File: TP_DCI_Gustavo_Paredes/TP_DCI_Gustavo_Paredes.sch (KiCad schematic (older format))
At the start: 32 parts, among them J101 Conector, J102 DB9 Hembra, J103 DB9 Macho, J104 Conector +5V, U101 LTC1485, U102 LTC1485

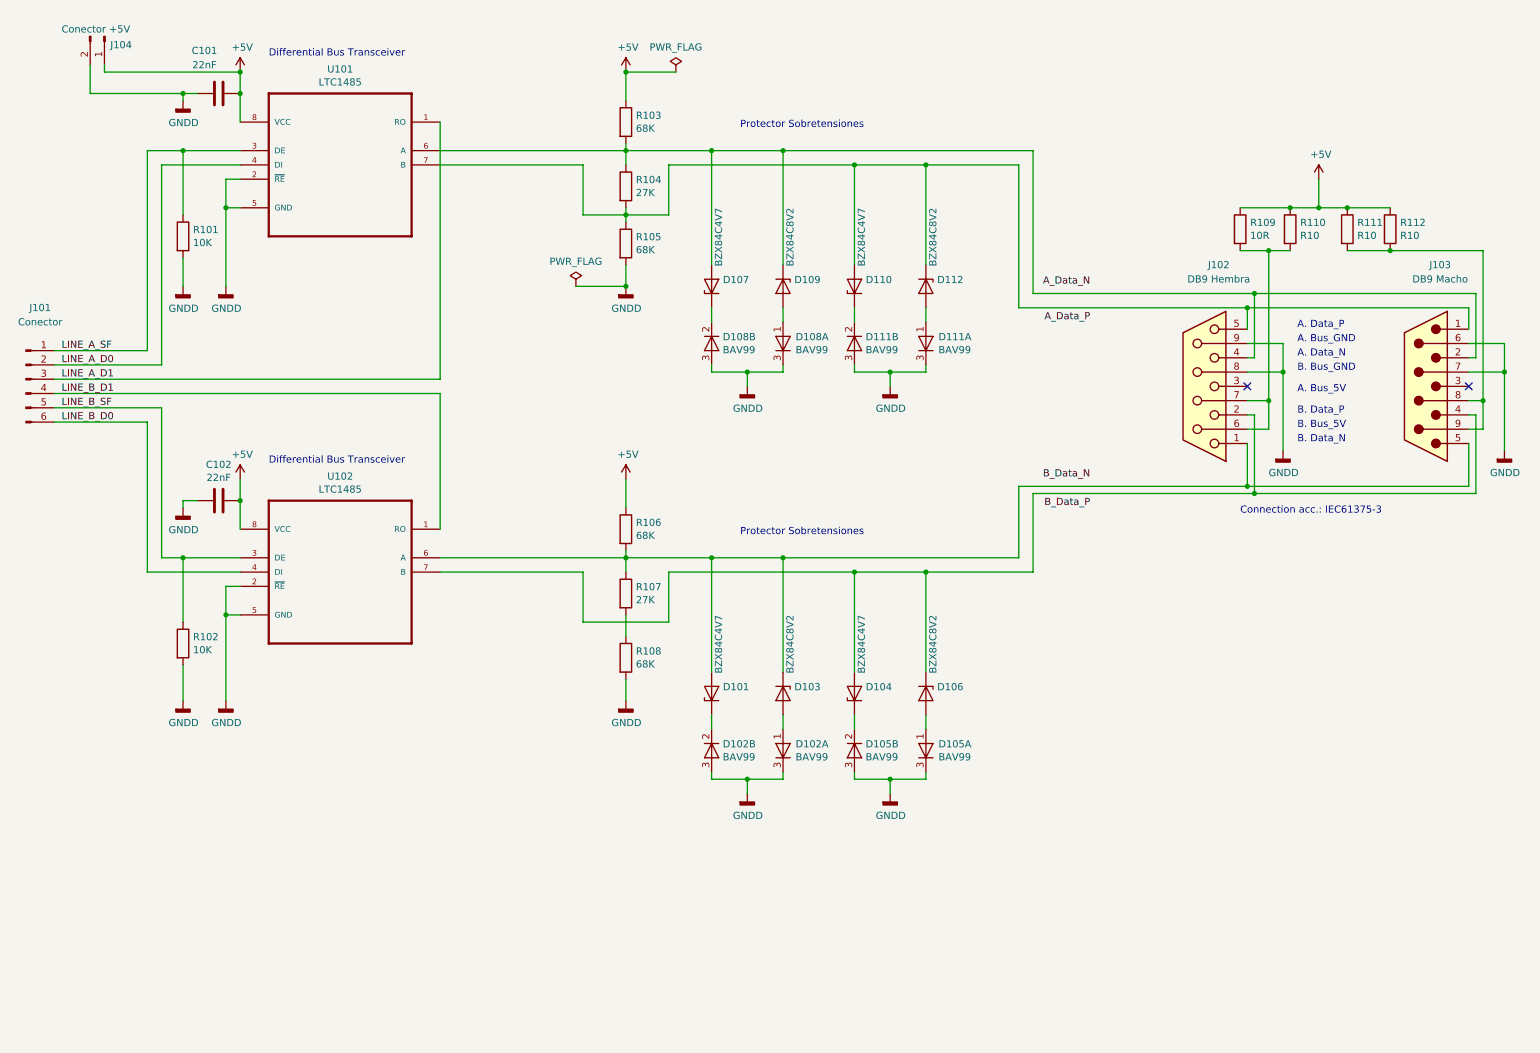
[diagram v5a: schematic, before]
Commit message: Correcciones Esquematico V3
Se realizaron las correcciones menores que el Docente indico. Se actualizo huella y 3D del LTC1485 y los dos DB9.
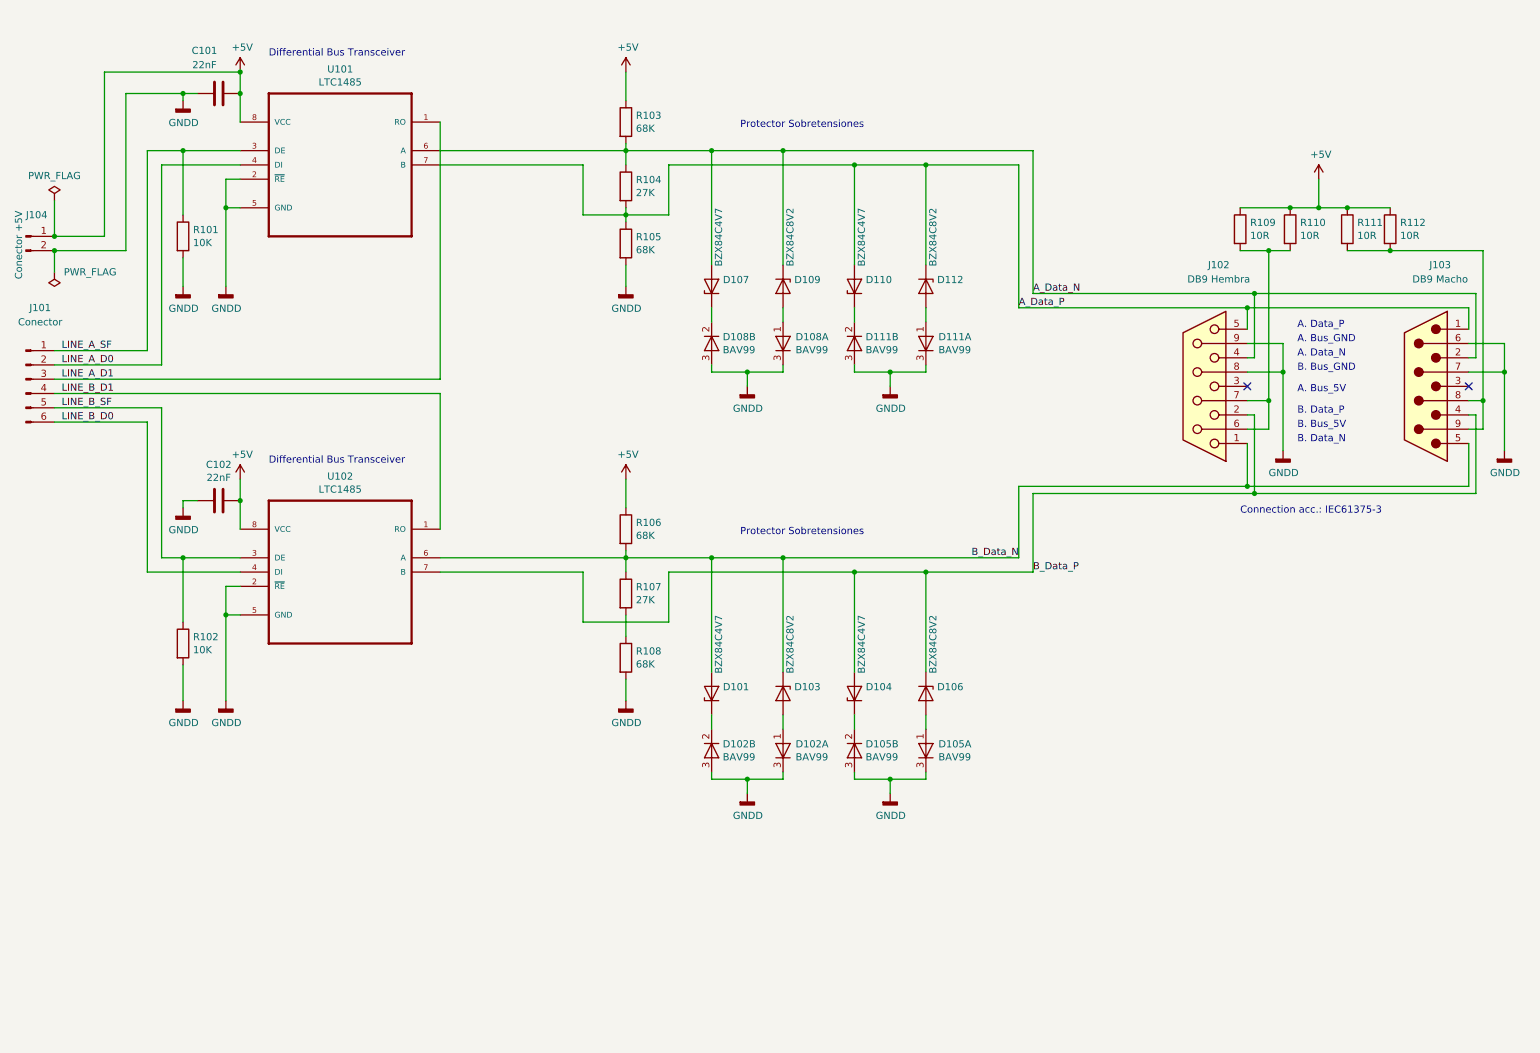
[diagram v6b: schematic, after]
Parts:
- J101: footprint Connector_PinHeader_1.00mm:PinHeader_1x06_P1.00mm_Vertical -> Connector_PinHeader_2.54mm:PinHeader_1x06_P2.54mm_Vertical
- J104: footprint Connector_PinHeader_1.00mm:PinHeader_1x02_P1.00mm_Vertical -> Connector_PinHeader_2.54mm:PinHeader_1x02_P2.54mm_Vertical
- R110, R111, R112: value R10 -> 10R
- U101, U102: footprint LTC1485IS8PBF:SOIC127P600X175-8N -> Package_DIP:DIP-8_W7.62mm_LongPads
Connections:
- net A_Data_N: now also D107.2 (A), D109.1 (K), J102.4, J103.2, R103.2, R104.1, U101.6 (A)
- net A_Data_P: now also D110.2 (A), D112.1 (K), J102.5, J103.1, R104.2, R105.1, U101.7 (B)
- net B_Data_N: now also D101.2 (A), D103.1 (K), J102.1, J103.5, R106.2, R107.1, U102.6 (A)
- net B_Data_P: now also D104.2 (A), D106.1 (K), J102.2, J103.4, U102.7 (B)
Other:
- moved on the sheet: J104
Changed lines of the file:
@@
 Sheet 1 1
 Title "KP99S RS485 PORT - Pagina 7/7"
-Date "2019-06-17"
-Rev "V2"
-Comp "CESE UBA - 7ma Cohorte"
+Date "2019-07-02"
+Rev "V3"
+Comp "DCI - CESE UBA - 7ma Cohorte"
 Comment1 "Autor: Gustavo Fabian Paredes Delaloye"
 Comment2 "Revisor: Julian Bustamante"
-Comment3 ""
+Comment3 "Licencia: GPL"
 Comment4 ""
 $EndDescr
@@
 F 0 "U101" H 2850 2170 50  0000 C CNN
 F 1 "LTC1485" H 2850 2079 50  0000 C CNN
-F 2 "LTC1485IS8PBF:SOIC127P600X175-8N" H 2850 1600 50  0001 L BNN
+F 2 "Package_DIP:DIP-8_W7.62mm_LongPads" H 2850 1600 50  0001 L BNN
 F 3 "https://ar.mouser.com/datasheet/2/609/1485fb-1268232.pdf" H 2850 1600 50  0001 L BNN
 F 4 "584-LTC1485CN8#PBF" H 2850 1600 50  0001 L BNN "MouserPartNumber"
@@
 F 0 "U102" H 2850 5020 50  0000 C CNN
 F 1 "LTC1485" H 2850 4929 50  0000 C CNN
-F 2 "LTC1485IS8PBF:SOIC127P600X175-8N" H 2850 4450 50  0001 L BNN
+F 2 "Package_DIP:DIP-8_W7.62mm_LongPads" H 2850 4450 50  0001 L BNN
 F 3 "https://ar.mouser.com/datasheet/2/609/1485fb-1268232.pdf" H 2850 4450 50  0001 L BNN
 F 4 "584-LTC1485CN8#PBF" H 2850 4450 50  0001 L BNN "MouserPartNumber"
@@
 L power:PWR_FLAG #FLG0101
 U 1 1 5D294E70
-P 5200 1050
-F 0 "#FLG0101" H 5200 1125 50  0001 C CNN
-F 1 "PWR_FLAG" H 5200 1224 50  0000 C CNN
-F 2 "" H 5200 1050 50  0001 C CNN
-F 3 "~" H 5200 1050 50  0001 C CNN
-	1    5200 1050
-	1    0    0    -1
-$EndComp
-Wire Wire Line
-	5200 1050 4850 1050
-Connection ~ 4850 1050
-Text Label 8100 3900 2    50   ~ 0
+P 850 1950
+F 0 "#FLG0101" H 850 2025 50  0001 C CNN
+F 1 "PWR_FLAG" H 850 2124 50  0000 C CNN
+F 2 "" H 850 1950 50  0001 C CNN
+F 3 "~" H 850 1950 50  0001 C CNN
+	1    850  1950
+	1    0    0    -1
+$EndComp
+Text Label 7600 4450 2    50   ~ 0
 B_Data_N
-Text Label 8100 4100 2    50   ~ 0
+Text Label 7700 4550 0    50   ~ 0
 B_Data_P
 Wire Wire Line
@@
 Wire Wire Line
 	5700 6000 5950 6000
-Text Label 8100 2550 2    50   ~ 0
+Text Label 7700 2600 0    50   ~ 0
 A_Data_N
-Text Label 8100 2800 2    50   ~ 0
+Text Label 7600 2700 0    50   ~ 0
 A_Data_P
 Wire Wire Line
@@
 P 9500 2150
 F 0 "R110" H 9570 2196 50  0000 L CNN
-F 1 "R10" H 9570 2105 50  0000 L CNN
+F 1 "10R" H 9570 2105 50  0000 L CNN
 F 2 "Resistor_THT:R_Axial_DIN0204_L3.6mm_D1.6mm_P5.08mm_Horizontal" V 9430 2150 50  0001 C CNN
 F 3 "~" H 9500 2150 50  0001 C CNN
@@
 P 10200 2150
 F 0 "R112" H 10270 2196 50  0000 L CNN
-F 1 "R10" H 10270 2105 50  0000 L CNN
+F 1 "10R" H 10270 2105 50  0000 L CNN
 F 2 "Resistor_THT:R_Axial_DIN0204_L3.6mm_D1.6mm_P5.08mm_Horizontal" V 10130 2150 50  0001 C CNN
 F 3 "~" H 10200 2150 50  0001 C CNN
@@
 P 9900 2150
 F 0 "R111" H 9970 2196 50  0000 L CNN
-F 1 "R10" H 9970 2105 50  0000 L CNN
+F 1 "10R" H 9970 2105 50  0000 L CNN
 F 2 "Resistor_THT:R_Axial_DIN0204_L3.6mm_D1.6mm_P5.08mm_Horizontal" V 9830 2150 50  0001 C CNN
 F 3 "~" H 9900 2150 50  0001 C CNN
@@
 F 0 "J101" H 750 3700 50  0000 C CNN
 F 1 "Conector" H 750 3600 50  0000 C CNN
-F 2 "Connector_PinHeader_1.00mm:PinHeader_1x06_P1.00mm_Vertical" H 650 3200 50  0001 C CNN
+F 2 "Connector_PinHeader_2.54mm:PinHeader_1x06_P2.54mm_Vertical" H 650 3200 50  0001 C CNN
 F 3 "~" H 650 3200 50  0001 C CNN
 	1    650  3200
@@
 L power:PWR_FLAG #FLG0102
 U 1 1 5D3E4B4C
-P 4500 2550
-F 0 "#FLG0102" H 4500 2625 50  0001 C CNN
-F 1 "PWR_FLAG" H 4500 2724 50  0000 C CNN
-F 2 "" H 4500 2550 50  0001 C CNN
-F 3 "~" H 4500 2550 50  0001 C CNN
-	1    4500 2550
-	1    0    0    -1
-$EndComp
-Wire Wire Line
-	4850 2550 4500 2550
-Connection ~ 4850 2550
+P 850 2450
+F 0 "#FLG0102" H 850 2525 50  0001 C CNN
+F 1 "PWR_FLAG" H 600 2450 50  0000 C CNN
+F 2 "" H 850 2450 50  0001 C CNN
+F 3 "~" H 850 2450 50  0001 C CNN
+	1    850  2450
+	-1   0    0    1
+$EndComp
 $Comp
 L Device:D_Zener D107
@@
 L Connector:Conn_01x02_Male J104
 U 1 1 5D4086E9
-P 1200 800
-F 0 "J104" V 1260 841 50  0000 L CNN
-F 1 "Conector +5V" V 1150 500 50  0000 L CNN
-F 2 "Connector_PinHeader_1.00mm:PinHeader_1x02_P1.00mm_Vertical" H 1200 800 50  0001 C CNN
-F 3 "~" H 1200 800 50  0001 C CNN
-	1    1200 800
-	0    1    1    0
-$EndComp
-Wire Wire Line
-	2150 1050 1200 1050
-Wire Wire Line
-	1200 1050 1200 1000
+P 650 2200
+F 0 "J104" H 650 2350 50  0000 L CNN
+F 1 "Conector +5V" V 600 1900 50  0000 L CNN
+F 2 "Connector_PinHeader_2.54mm:PinHeader_1x02_P2.54mm_Vertical" H 650 2200 50  0001 C CNN
+F 3 "~" H 650 2200 50  0001 C CNN
+	1    650  2200
+	1    0    0    -1
+$EndComp
 Connection ~ 2150 1050
-Wire Wire Line
-	1750 1200 1100 1200
-Wire Wire Line
-	1100 1200 1100 1000
 Connection ~ 1750 1200
+Wire Wire Line
+	1200 1050 2150 1050
+Wire Wire Line
+	850  2200 1200 2200
+Wire Wire Line
+	1200 2200 1200 1050
+Wire Wire Line
+	850  2300 1350 2300
+Wire Wire Line
+	1350 2300 1350 1200
+Wire Wire Line
+	1350 1200 1750 1200
+Wire Wire Line
+	850  1950 850  2200
+Connection ~ 850  2200
+Connection ~ 850  2300
+Wire Wire Line
+	850  2450 850  2300
 $EndSCHEMATC

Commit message: PCB V1
Se termina V1 del PCB a la espera de las correcciones.
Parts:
- added H101, H102, H103, H104: MountingHole, N_A, symbol Mechanical:MountingHole
- C101, C102: symbol Device:C -> TP_DCI_Gustavo_Paredes-rescue:C-Device
- D101, D103, D104, D106, D107, D109, D110, D112: symbol Device:D_Zener -> TP_DCI_Gustavo_Paredes-rescue:D_Zener-Device
- D102, D105, D108, D111: symbol Diode:BAV99 -> TP_DCI_Gustavo_Paredes-rescue:BAV99-Diode
- J101: symbol Connector:Conn_01x06_Male -> TP_DCI_Gustavo_Paredes-rescue:Conn_01x06_Male-Connector
- J102: symbol Connector:DB9_Female -> TP_DCI_Gustavo_Paredes-rescue:DB9_Female-Connector
- J103: symbol Connector:DB9_Male -> TP_DCI_Gustavo_Paredes-rescue:DB9_Male-Connector
- J104: symbol Connector:Conn_01x02_Male -> TP_DCI_Gustavo_Paredes-rescue:Conn_01x02_Male-Connector
- R101, R102, R103, R104, R105, R106, R107, R108, R109, R110, R111, R112: symbol Device:R -> TP_DCI_Gustavo_Paredes-rescue:R-Device
- U101, U102: symbol LTC1485IS8PBF:LTC1485IS8PBF -> TP_DCI_Gustavo_Paredes-rescue:LTC1485IS8PBF-LTC1485IS8PBF

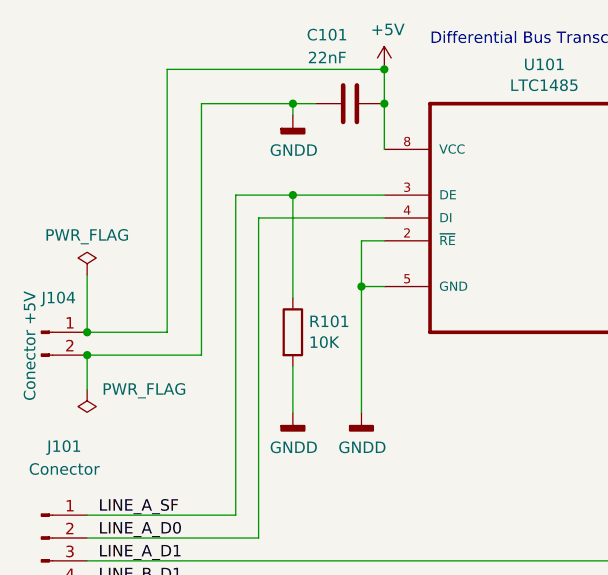
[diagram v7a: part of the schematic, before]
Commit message: Correccion Esquematico
Correccion del esquematico en conector J104.
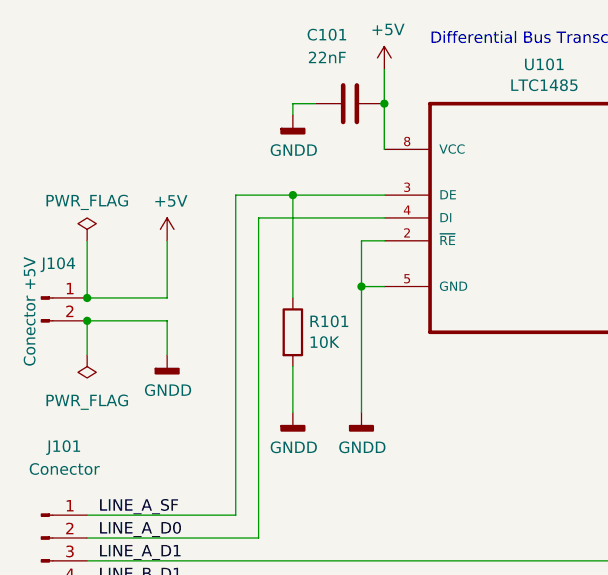
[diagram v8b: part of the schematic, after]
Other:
- moved on the sheet: J104
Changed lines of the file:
@@
 L TP_DCI_Gustavo_Paredes-rescue:PWR_FLAG-power #FLG0101
 U 1 1 5D294E70
-P 850 1950
-F 0 "#FLG0101" H 850 2025 50  0001 C CNN
-F 1 "PWR_FLAG" H 850 2124 50  0000 C CNN
-F 2 "" H 850 1950 50  0001 C CNN
-F 3 "~" H 850 1950 50  0001 C CNN
-	1    850  1950
+P 850 1800
+F 0 "#FLG0101" H 850 1875 50  0001 C CNN
+F 1 "PWR_FLAG" H 850 1974 50  0000 C CNN
+F 2 "" H 850 1800 50  0001 C CNN
+F 3 "~" H 850 1800 50  0001 C CNN
+	1    850  1800
 	1    0    0    -1
 $EndComp
@@
 L TP_DCI_Gustavo_Paredes-rescue:PWR_FLAG-power #FLG0102
 U 1 1 5D3E4B4C
-P 850 2450
-F 0 "#FLG0102" H 850 2525 50  0001 C CNN
-F 1 "PWR_FLAG" H 600 2450 50  0000 C CNN
-F 2 "" H 850 2450 50  0001 C CNN
-F 3 "~" H 850 2450 50  0001 C CNN
-	1    850  2450
+P 850 2300
+F 0 "#FLG0102" H 850 2375 50  0001 C CNN
+F 1 "PWR_FLAG" H 850 2500 50  0000 C CNN
+F 2 "" H 850 2300 50  0001 C CNN
+F 3 "~" H 850 2300 50  0001 C CNN
+	1    850  2300
 	-1   0    0    1
 $EndComp
@@
 L TP_DCI_Gustavo_Paredes-rescue:Conn_01x02_Male-Connector J104
 U 1 1 5D4086E9
-P 650 2200
-F 0 "J104" H 650 2350 50  0000 L CNN
-F 1 "Conector +5V" V 600 1900 50  0000 L CNN
-F 2 "Connector_PinHeader_2.54mm:PinHeader_1x02_P2.54mm_Vertical" H 650 2200 50  0001 C CNN
-F 3 "~" H 650 2200 50  0001 C CNN
-	1    650  2200
-	1    0    0    -1
-$EndComp
-Connection ~ 2150 1050
-Connection ~ 1750 1200
-Wire Wire Line
-	1200 1050 2150 1050
-Wire Wire Line
-	850  2200 1200 2200
-Wire Wire Line
-	1200 2200 1200 1050
-Wire Wire Line
-	850  2300 1350 2300
-Wire Wire Line
-	1350 2300 1350 1200
-Wire Wire Line
-	1350 1200 1750 1200
-Wire Wire Line
-	850  1950 850  2200
-Connection ~ 850  2200
-Connection ~ 850  2300
-Wire Wire Line
-	850  2450 850  2300
+P 650 2050
+F 0 "J104" H 650 2200 50  0000 L CNN
+F 1 "Conector +5V" V 600 1750 50  0000 L CNN
+F 2 "Connector_PinHeader_2.54mm:PinHeader_1x02_P2.54mm_Vertical" H 650 2050 50  0001 C CNN
+F 3 "~" H 650 2050 50  0001 C CNN
+	1    650  2050
+	1    0    0    -1
+$EndComp
+Wire Wire Line
+	850  2050 1200 2050
+Wire Wire Line
+	850  2150 1200 2150
+Wire Wire Line
+	850  1800 850  2050
+Connection ~ 850  2050
+Connection ~ 850  2150
+Wire Wire Line
+	850  2300 850  2150
 $Comp
 L Mechanical:MountingHole H101
@@
 	1    0    0    -1
 $EndComp
+$Comp
+L TP_DCI_Gustavo_Paredes-rescue:GNDD-power #PWR?
+U 1 1 5D244500
+P 1200 2300
+F 0 "#PWR?" H 1200 2050 50  0001 C CNN
+F 1 "GNDD" H 1204 2145 50  0000 C CNN
+F 2 "" H 1200 2300 50  0001 C CNN
+F 3 "" H 1200 2300 50  0001 C CNN
+	1    1200 2300
+	1    0    0    -1
+$EndComp
+$Comp
+L TP_DCI_Gustavo_Paredes-rescue:+5V-power #PWR?
+U 1 1 5D24455B
+P 1200 1800
+F 0 "#PWR?" H 1200 1650 50  0001 C CNN
+F 1 "+5V" H 1215 1973 50  0000 C CNN
+F 2 "" H 1200 1800 50  0001 C CNN
+F 3 "" H 1200 1800 50  0001 C CNN
+	1    1200 1800
+	1    0    0    -1
+$EndComp
+Wire Wire Line
+	1200 2050 1200 1800
+Wire Wire Line
+	1200 2300 1200 2150
 $EndSCHEMATC
